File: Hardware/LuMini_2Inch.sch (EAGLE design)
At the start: 49 parts, among them J1 DOUBLE_LED_PAD, J2 DOUBLE_LED_PAD, J3 DOUBLE_LED_PAD

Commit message: adding silk
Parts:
- added LOGO1: OSHW-LOGOS, SparkFun-Aesthetics:OSHW-LOGOS
- added LOGO2: SFE_LOGO_NAME.1_INCH, SparkFun-Aesthetics:SFE_LOGO_NAME.1_INCH
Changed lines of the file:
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@@
 <part name="SUPPLY17" library="SparkFun-PowerSymbols" deviceset="5V" device=""/>
 <part name="GND42" library="SparkFun-PowerSymbols" deviceset="GND" device=""/>
+<part name="LOGO1" library="SparkFun-Aesthetics" deviceset="OSHW-LOGO" device="S"/>
+<part name="LOGO2" library="SparkFun-Aesthetics" deviceset="SFE_LOGO_NAME" device=".1_INCH"/>
 </parts>
 <sheets>
@@
 <instance part="SUPPLY17" gate="G$1" x="106.68" y="38.1"/>
 <instance part="GND42" gate="1" x="106.68" y="22.86"/>
+<instance part="LOGO1" gate="G$1" x="236.22" y="45.72"/>
+<instance part="LOGO2" gate="G$1" x="147.32" y="38.1"/>
 </instances>
 <busses>

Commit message: post checklist
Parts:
- added FD1, FD2, FD3, FD4: FIDUCIALUFIDUCIAL, SparkFun-Aesthetics:FIDUCIALUFIDUCIAL
- added H5, H6, H7, H8: STANDOFF_ELECTRICALSTANDOFF-ELECTRICAL-NOTHERMALS, SparkFun-Hardware:STANDOFF_ELECTRICALSTANDOFF-ELECTRICAL-NOTHERMALS
- C1: value 4.7uF -> DNP; device SparkFun-Capacitors:4.7UF-0603-6.3V-(10%) -> SparkFun-Capacitors:4.7UF-1206-16V-(+80/-20%)
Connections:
- net GND: now also H5.P$1, H6.P$1, H7.P$1, H8.P$1
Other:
- note added: "LED's"
- note added: "Optional Capacitor"
- note added: "Standoffs/Heatsinks"
- note added: "Vin: 3.0V-5.5V"
- moved on the sheet: C1, D1, D10, D11, D12, D13, D14, D15, D16, D17, D18, D19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

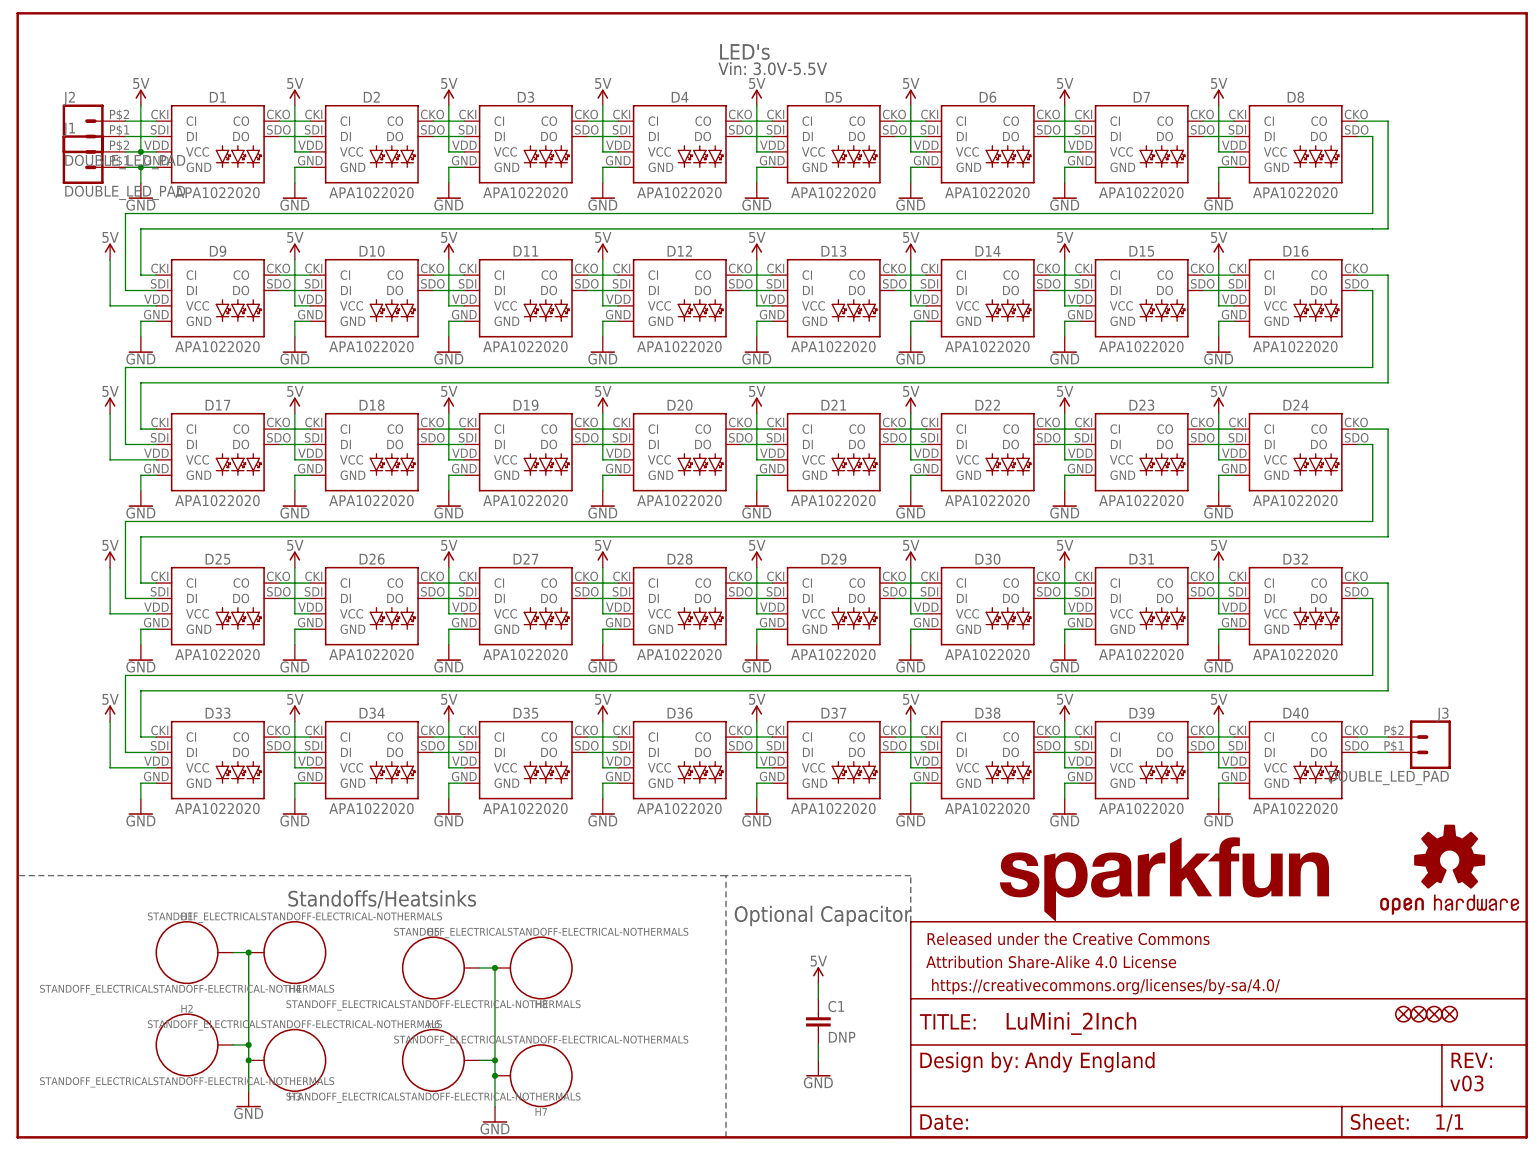
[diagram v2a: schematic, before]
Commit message: cleaning schematic
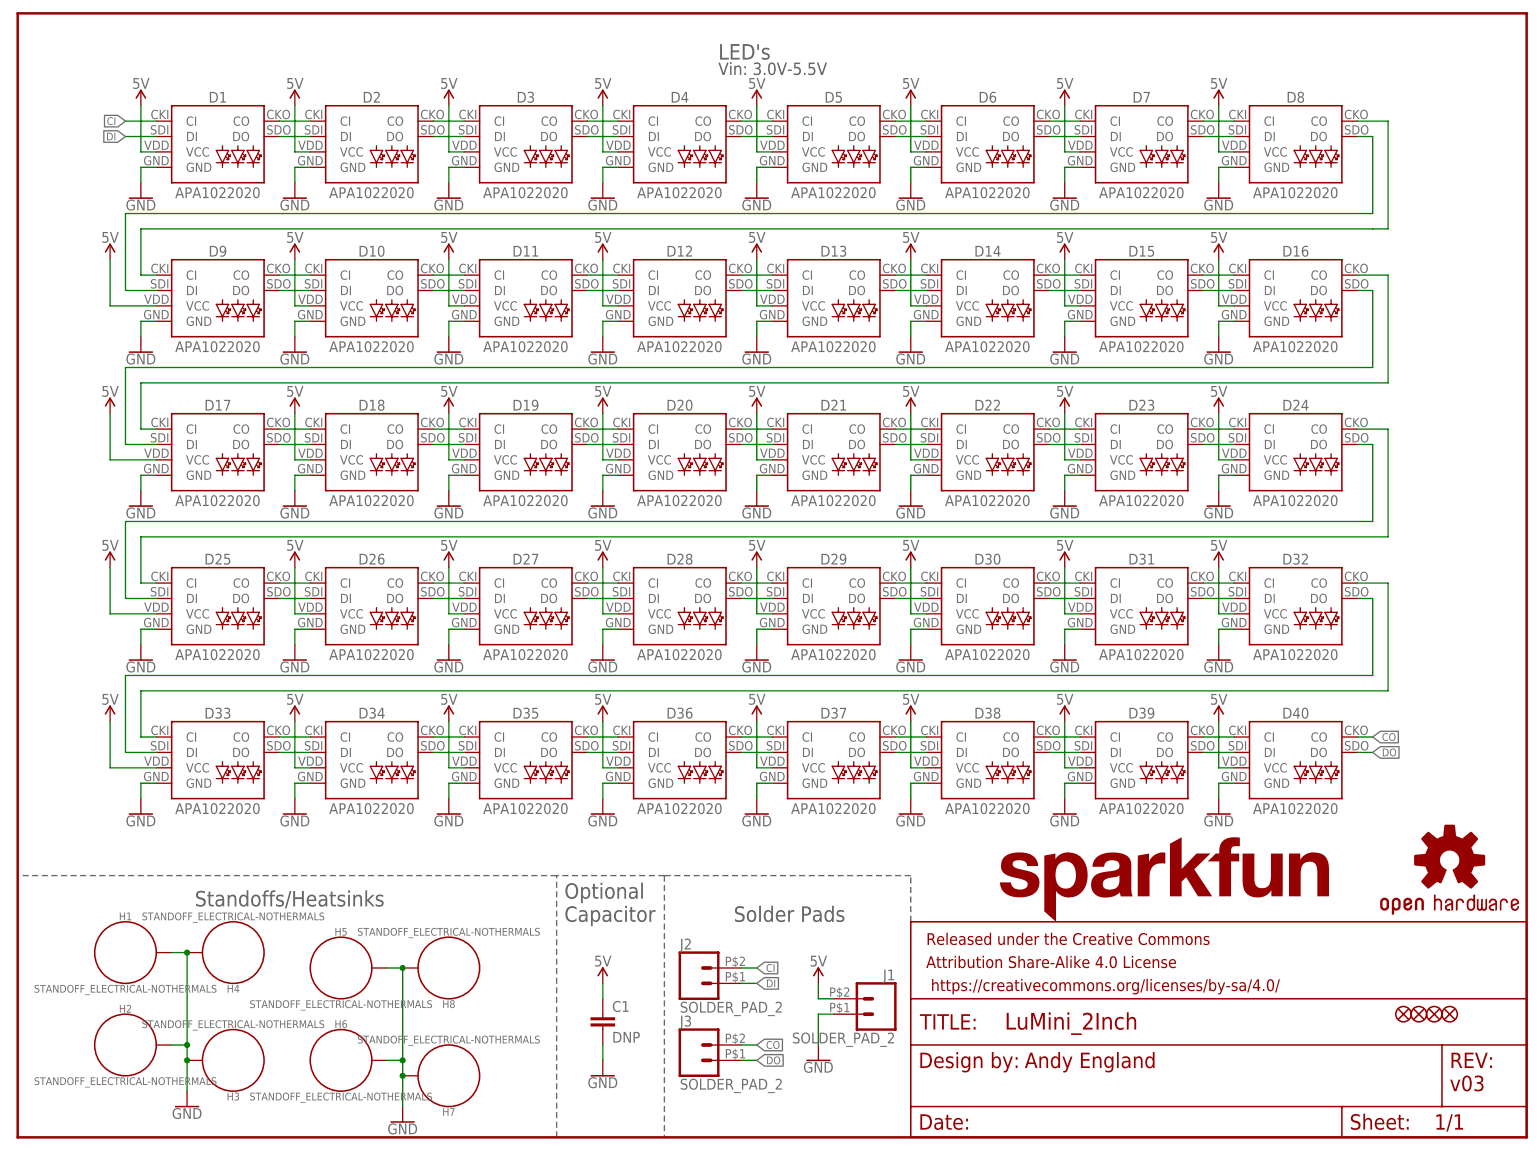
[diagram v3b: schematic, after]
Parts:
- H1, H2, H3, H4, H5, H6, H7, H8: value STANDOFF_ELECTRICALSTANDOFF-ELECTRICAL-NOTHERMALS -> STANDOFF_ELECTRICAL-NOTHERMALS; device SparkFun-Hardware:STANDOFF_ELECTRICALSTANDOFF-ELECTRICAL-NOTHERMALS -> SparkFun-Hardware:STANDOFF_ELECTRICAL-NOTHERMALS
- J1, J2, J3: value DOUBLE_LED_PAD -> SOLDER_PAD_2; device Andy:DOUBLE_LED_PAD -> SparkFun-Connectors:SOLDER_PAD_2
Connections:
- net N$133 renamed CO
- net N$134 renamed DO
- net N$2 renamed CI
- net N$3 renamed DI
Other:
- note added: "Solder Pads"
- moved on the sheet: C1, H1, H2, H3, H4, H5, H6, H7, H8, J1, J2, J3

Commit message: Updating to proper footprint
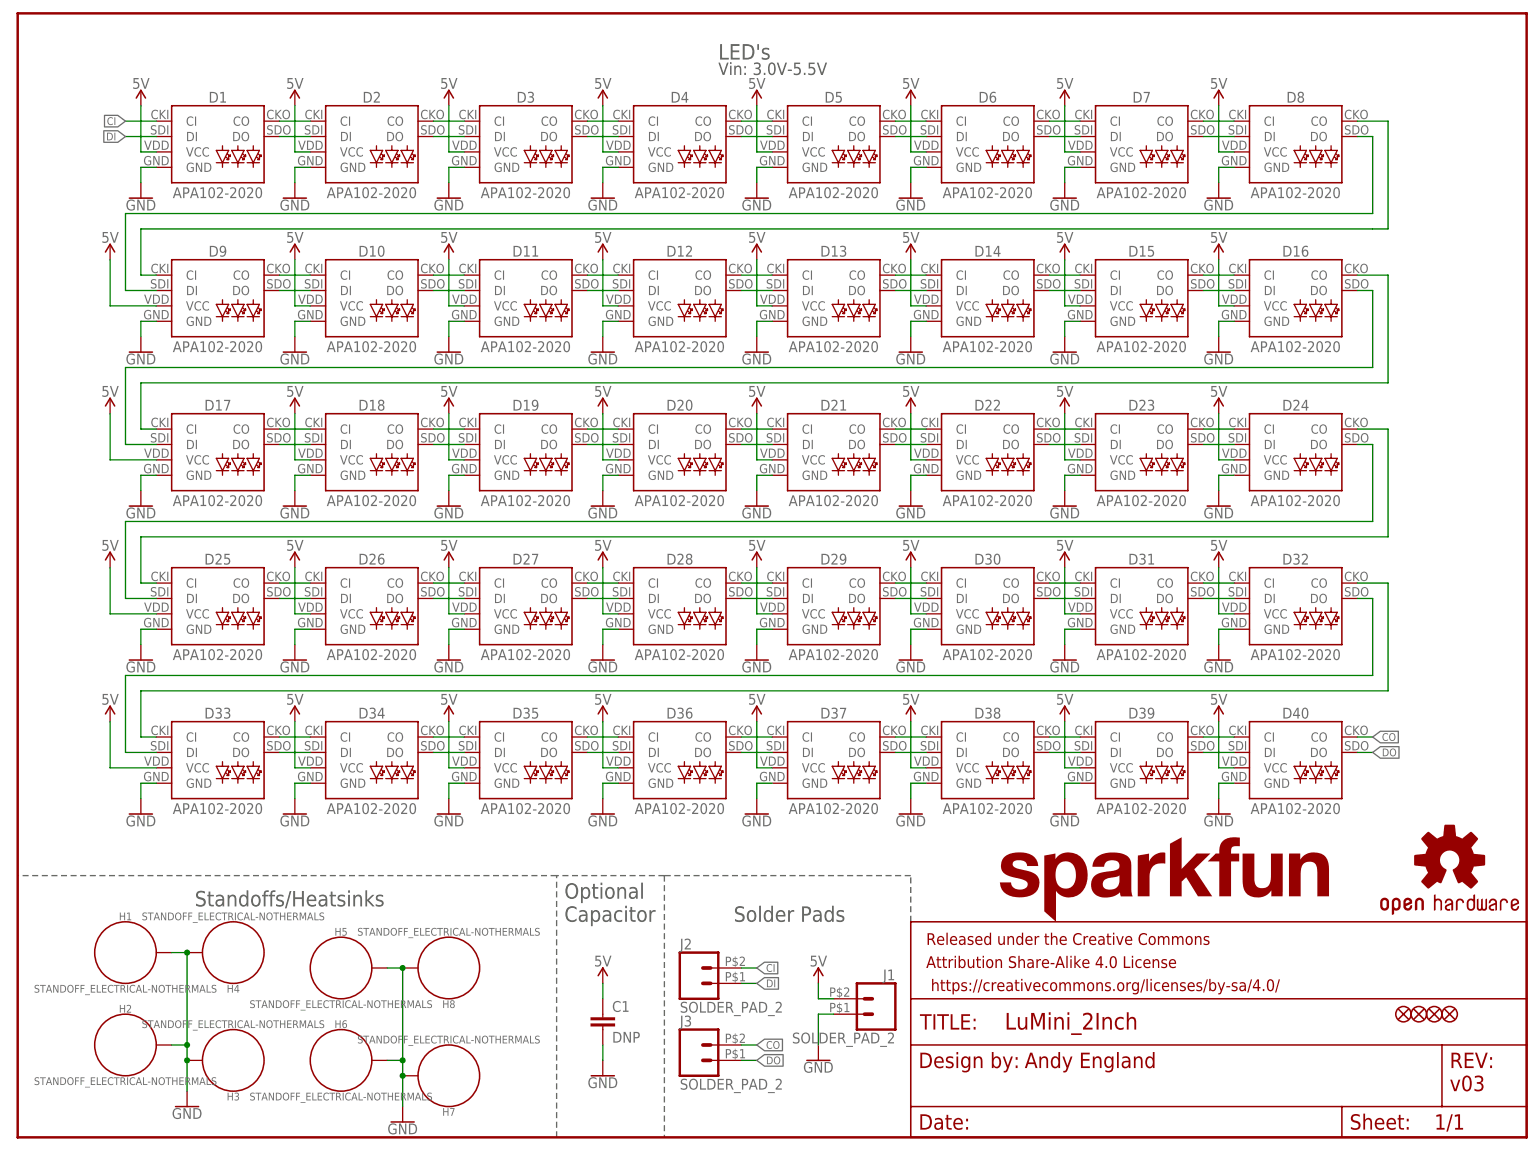
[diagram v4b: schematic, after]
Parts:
- D1, D10, D11, D12, D13, D14, D15, D16, D17, D18, D19, D2, D20, D21, D22, D23, D24, D25, D26, D27, D28, D29, D3, D30, D31, D32, D33, D34, D35, D36, D37, D38, D39, D4, D40, D5, D6, D7, D8, D9: value APA1022020 -> APA102-2020; device SparkFun-LED:APA1022020 -> SparkFun-LED:APA102-2020

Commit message: version number change
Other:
- note added: "v10"
- note removed: "v03"
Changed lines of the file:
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@@
 <sheet>
 <plain>
-<text x="236.22" y="7.62" size="2.54" layer="94" font="vector">v03</text>
+<text x="236.22" y="7.62" size="2.54" layer="94" font="vector">v10</text>
 <text x="166.116" y="11.43" size="2.54" layer="94" font="vector">Andy England</text>
 <wire x1="147.32" y1="35.56" x2="147.32" y2="43.18" width="0.2032" layer="97" style="longdash"/>
